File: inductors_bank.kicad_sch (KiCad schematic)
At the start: 38 parts, among them K501 HF3F-L-12-1ZL2T, K502 HF3F-L-12-1ZL2T, K503 HF3F-L-12-1ZL2T, K504 HF3F-L-12-1ZL2T, K505 HF3F-L-12-1ZL2T, K506 HF3F-L-12-1ZL2T, K507 HF3F-L-12-1ZL2T, Q501 PMOS, Q502 PMOS, Q503 NMOS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

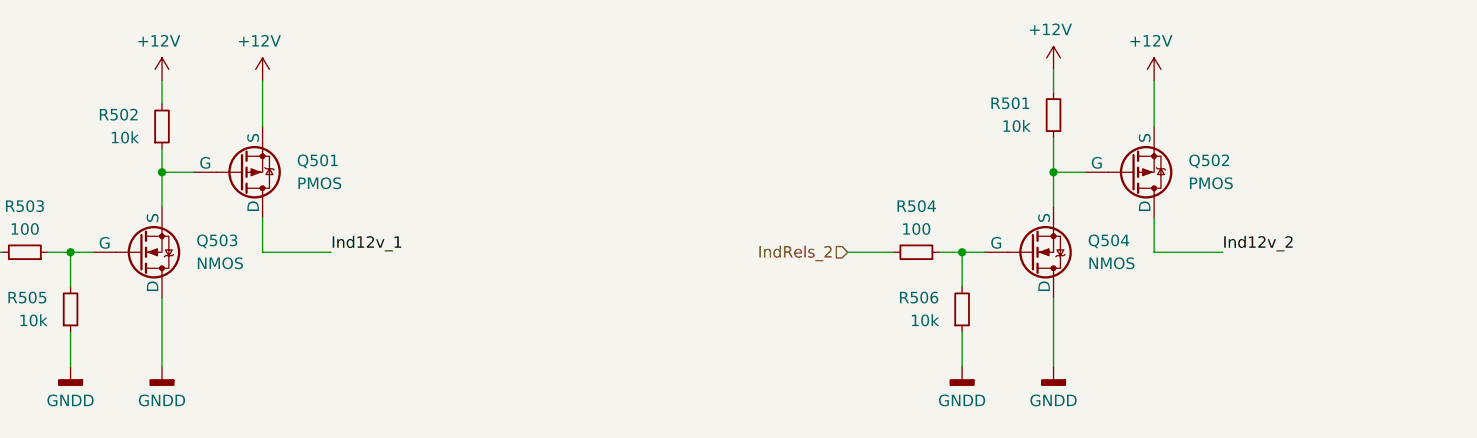
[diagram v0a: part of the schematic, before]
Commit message: Many more vias, improved some routing
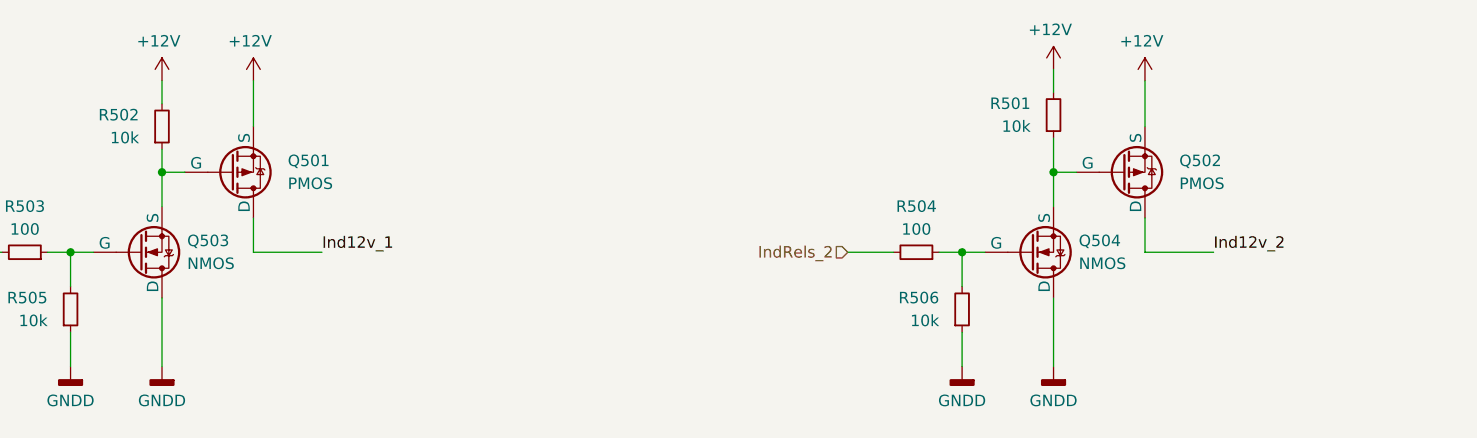
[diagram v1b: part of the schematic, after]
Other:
- moved on the sheet: Q501, Q502
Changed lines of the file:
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@@
 	(wire
 		(pts
-			(xy 211.836 57.15) (xy 211.836 62.23)
+			(xy 210.82 57.15) (xy 210.82 62.23)
 		)
 		(stroke
@@
 	(wire
 		(pts
-			(xy 112.776 57.15) (xy 112.776 62.23)
+			(xy 111.76 57.15) (xy 111.76 62.23)
 		)
 		(stroke
@@
 	(wire
 		(pts
-			(xy 211.836 76.2) (xy 211.836 72.39)
+			(xy 210.82 76.2) (xy 210.82 72.39)
 		)
 		(stroke
@@
 	(wire
 		(pts
-			(xy 204.216 67.31) (xy 200.66 67.31)
+			(xy 203.2 67.31) (xy 200.66 67.31)
 		)
 		(stroke
@@
 	(wire
 		(pts
-			(xy 105.156 67.31) (xy 101.6 67.31)
+			(xy 104.14 67.31) (xy 101.6 67.31)
 		)
 		(stroke
@@
 	(wire
 		(pts
-			(xy 120.396 76.2) (xy 112.776 76.2)
+			(xy 119.38 76.2) (xy 111.76 76.2)
 		)
 		(stroke
@@
 	(wire
 		(pts
-			(xy 219.456 76.2) (xy 211.836 76.2)
+			(xy 218.44 76.2) (xy 210.82 76.2)
 		)
 		(stroke
@@
 	(wire
 		(pts
-			(xy 112.776 76.2) (xy 112.776 72.39)
+			(xy 111.76 76.2) (xy 111.76 72.39)
 		)
 		(stroke
@@
 	)
 	(label "Ind12v_2"
-		(at 219.456 76.2 0)
+		(at 218.44 76.2 0)
 		(fields_autoplaced yes)
 		(effects
@@
 	)
 	(label "Ind12v_1"
-		(at 120.396 76.2 0)
+		(at 119.38 76.2 0)
 		(fields_autoplaced yes)
 		(effects
@@
 		(on_board yes)
 		(dnp no)
-		(fields_autoplaced yes)
 		(property "Reference" "Q504"
-			(at 204.47 74.9299 0)
+			(at 203.454 74.9299 0)
 			(effects
 				(font
@@
 		)
 		(property "Value" "NMOS"
-			(at 204.47 77.4699 0)
+			(at 203.454 77.4699 0)
 			(effects
 				(font
@@
 	(symbol
 		(lib_id "power:+12V")
-		(at 112.776 57.15 0)
+		(at 111.76 57.15 0)
 		(mirror y)
 		(unit 1)
@@
 		(dnp no)
 		(property "Reference" "#PWR0503"
-			(at 112.776 60.96 0)
+			(at 111.76 60.96 0)
 			(effects
 				(font
@@
 		)
 		(property "Value" "+12V"
-			(at 112.395 52.7558 0)
+			(at 111.379 52.7558 0)
 			(effects
 				(font
@@
 		)
 		(property "Footprint" ""
-			(at 112.776 57.15 0)
+			(at 111.76 57.15 0)
 			(effects
 				(font
@@
 		)
 		(property "Datasheet" ""
-			(at 112.776 57.15 0)
+			(at 111.76 57.15 0)
 			(effects
 				(font
@@
 		)
 		(property "Description" "Power symbol creates a global label with name \"+12V\""
-			(at 112.776 57.15 0)
+			(at 111.76 57.15 0)
 			(effects
 				(font
@@
 	(symbol
 		(lib_id "Simulation_SPICE:PMOS")
-		(at 209.296 67.31 0)
+		(at 208.28 67.31 0)
 		(mirror x)
 		(unit 1)
@@
 		(fields_autoplaced yes)
 		(property "Reference" "Q502"
-			(at 215.646 66.0399 0)
+			(at 214.63 66.0399 0)
 			(effects
 				(font
@@
 		)
 		(property "Value" "PMOS"
-			(at 215.646 68.5799 0)
+			(at 214.63 68.5799 0)
 			(effects
 				(font
@@
 		)
 		(property "Footprint" "Package_TO_SOT_SMD:SOT-23"
-			(at 214.376 69.85 0)
+			(at 213.36 69.85 0)
 			(effects
 				(font
@@
 		)
 		(property "Datasheet" "https://ngspice.sourceforge.io/docs/ngspice-html-manual/manual.xhtml#cha_MOSFETs"
-			(at 209.296 54.61 0)
+			(at 208.28 54.61 0)
 			(effects
 				(font
@@
 		)
 		(property "Description" "P-MOSFET transistor, drain/source/gate"
-			(at 209.296 67.31 0)
+			(at 208.28 67.31 0)
 			(effects
 				(font
@@
 		)
 		(property "Sim.Device" "PMOS"
-			(at 209.296 50.165 0)
+			(at 208.28 50.165 0)
 			(effects
 				(font
@@
 		)
 		(property "Sim.Type" "VDMOS"
-			(at 209.296 48.26 0)
+			(at 208.28 48.26 0)
 			(effects
 				(font
@@
 		)
 		(property "Sim.Pins" "1=D 2=G 3=S"
-			(at 209.296 52.07 0)
+			(at 208.28 52.07 0)
 			(effects
 				(font
@@
 	(symbol
 		(lib_id "Simulation_SPICE:PMOS")
-		(at 110.236 67.31 0)
+		(at 109.22 67.31 0)
 		(mirror x)
 		(unit 1)
@@
 		(fields_autoplaced yes)
 		(property "Reference" "Q501"
-			(at 116.586 66.0399 0)
+			(at 115.57 66.0399 0)
 			(effects
 				(font
@@
 		)
 		(property "Value" "PMOS"
-			(at 116.586 68.5799 0)
+			(at 115.57 68.5799 0)
 			(effects
 				(font
@@
 		)
 		(property "Footprint" "Package_TO_SOT_SMD:SOT-23"
-			(at 115.316 69.85 0)
+			(at 114.3 69.85 0)
 			(effects
 				(font
@@
 		)
 		(property "Datasheet" "https://ngspice.sourceforge.io/docs/ngspice-html-manual/manual.xhtml#cha_MOSFETs"
-			(at 110.236 54.61 0)
+			(at 109.22 54.61 0)
 			(effects
 				(font
@@
 		)
 		(property "Description" "P-MOSFET transistor, drain/source/gate"
-			(at 110.236 67.31 0)
+			(at 109.22 67.31 0)
 			(effects
 				(font
@@
 		)
 		(property "Sim.Device" "PMOS"
-			(at 110.236 50.165 0)
+			(at 109.22 50.165 0)
 			(effects
 				(font
@@
 		)
 		(property "Sim.Type" "VDMOS"
-			(at 110.236 48.26 0)
+			(at 109.22 48.26 0)
 			(effects
 				(font
@@
 		)
 		(property "Sim.Pins" "1=D 2=G 3=S"
-			(at 110.236 52.07 0)
+			(at 109.22 52.07 0)
 			(effects
 				(font
@@
 	(symbol
 		(lib_id "power:+12V")
-		(at 211.836 57.15 0)
+		(at 210.82 57.15 0)
 		(mirror y)
 		(unit 1)
@@
 		(dnp no)
 		(property "Reference" "#PWR0504"
-			(at 211.836 60.96 0)
+			(at 210.82 60.96 0)
 			(effects
 				(font
@@
 		)
 		(property "Value" "+12V"
-			(at 211.455 52.7558 0)
+			(at 210.439 52.7558 0)
 			(effects
 				(font
@@
 		)
 		(property "Footprint" ""
-			(at 211.836 57.15 0)
+			(at 210.82 57.15 0)
 			(effects
 				(font
@@
 		)
 		(property "Datasheet" ""
-			(at 211.836 57.15 0)
+			(at 210.82 57.15 0)
 			(effects
 				(font
@@
 		)
 		(property "Description" "Power symbol creates a global label with name \"+12V\""
-			(at 211.836 57.15 0)
+			(at 210.82 57.15 0)
 			(effects
 				(font
@@
 		(on_board yes)
 		(dnp no)
-		(fields_autoplaced yes)
 		(property "Reference" "Q503"
-			(at 105.41 74.9299 0)
+			(at 104.394 74.9299 0)
 			(effects
 				(font
@@
 		)
 		(property "Value" "NMOS"
-			(at 105.41 77.4699 0)
+			(at 104.394 77.4699 0)
 			(effects
 				(font

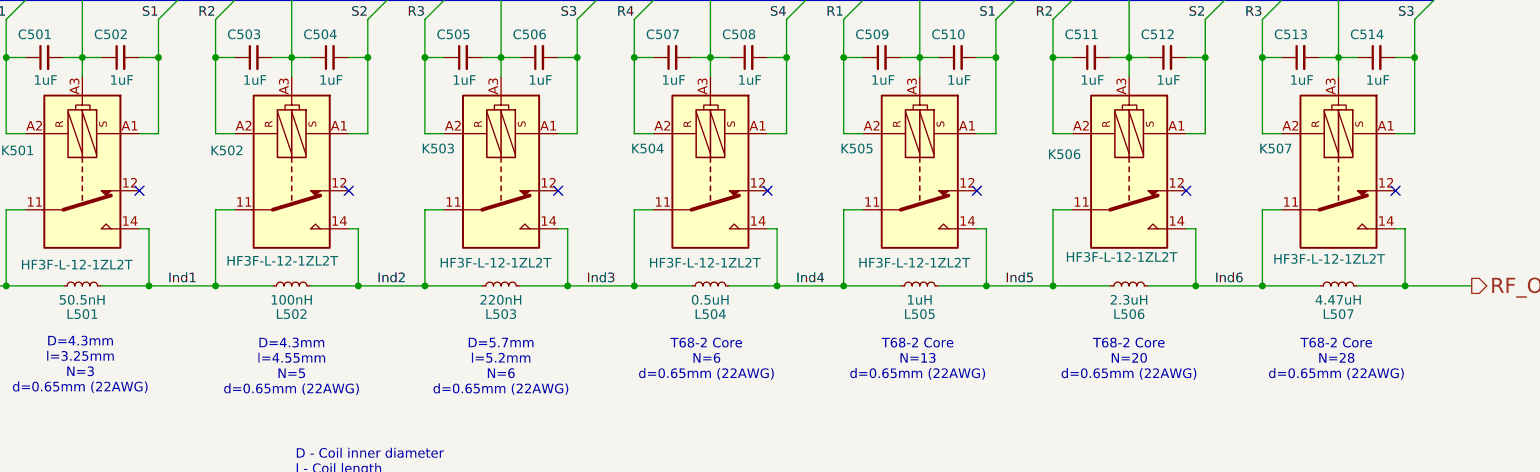
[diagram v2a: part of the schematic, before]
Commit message: Improve RF routing
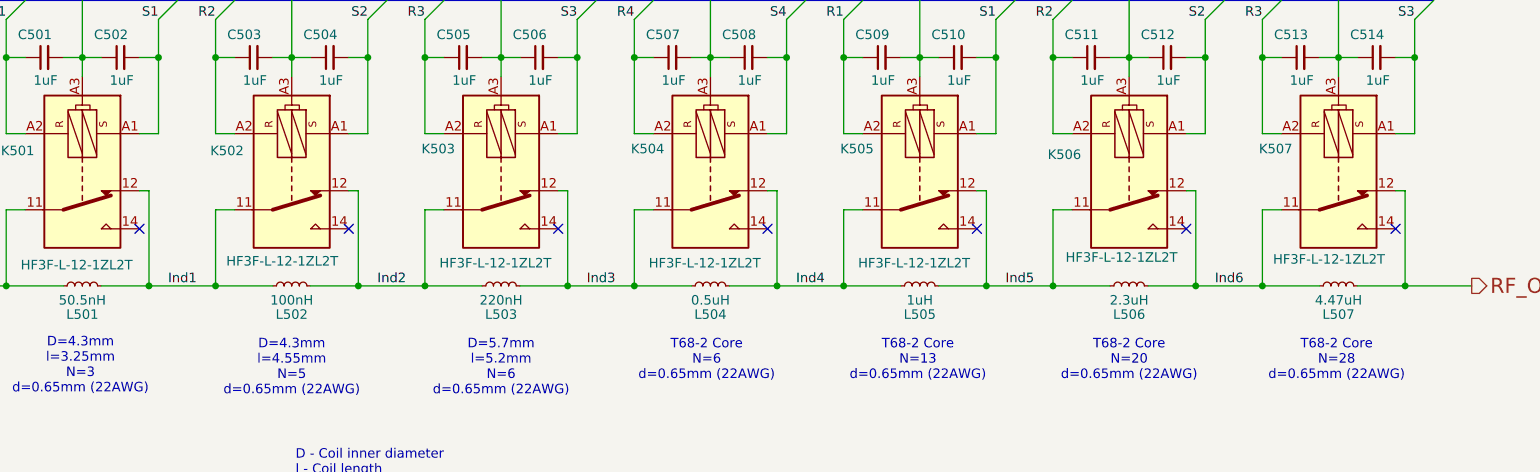
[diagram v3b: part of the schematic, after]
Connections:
- net Ind1: now also K501.12; no longer K501.14
- net Ind2: now also K502.12; no longer K502.14
- net Ind3: now also K503.12; no longer K503.14
- net Ind4: now also K504.12; no longer K504.14
- net Ind5: now also K505.12; no longer K505.14
- net Ind6: now also K506.12; no longer K506.14
- net RF_Out: now also K507.12; no longer K507.14

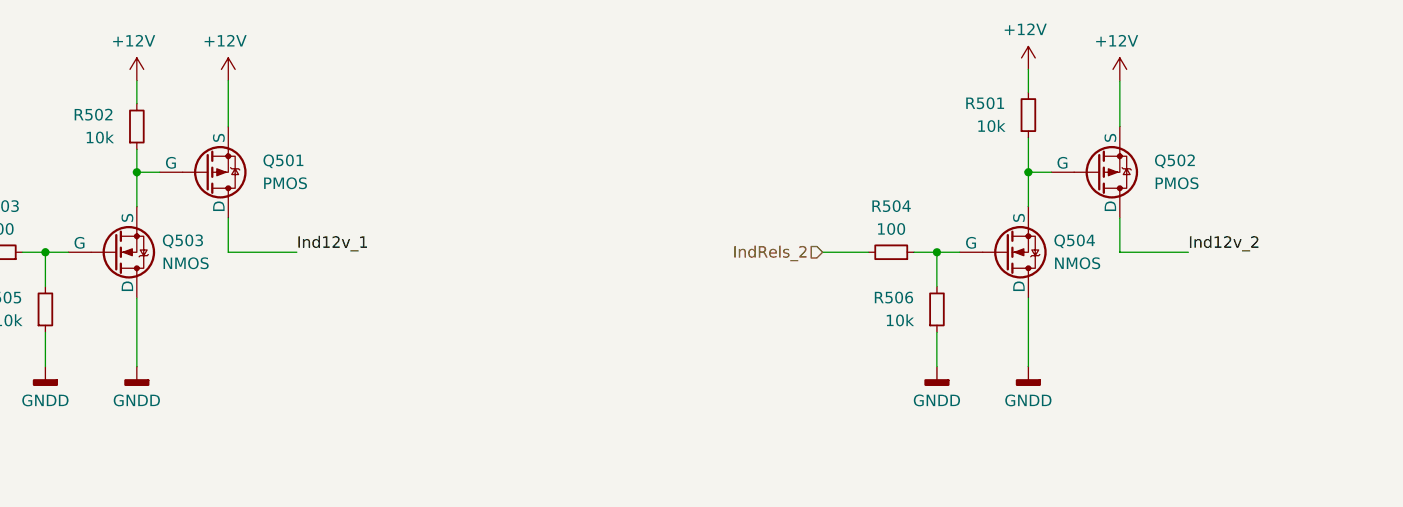
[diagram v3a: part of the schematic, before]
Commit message: Added transistors parts. Added reverse polarity protection, pending adding to layout
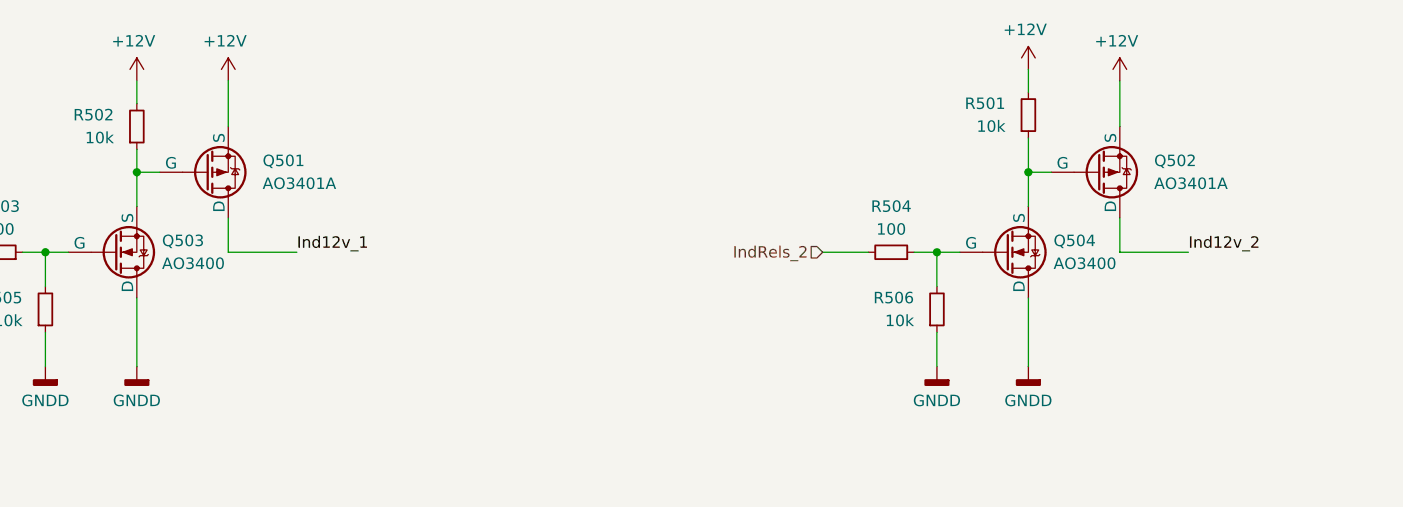
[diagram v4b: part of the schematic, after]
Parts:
- Q501, Q502: value PMOS -> AO3401A
- Q503, Q504: value NMOS -> AO3400
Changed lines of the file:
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@@
 			)
 		)
-		(property "Value" "NMOS"
+		(property "Value" "AO3400"
 			(at 203.454 77.4699 0)
 			(effects
@@
 			)
 		)
-		(property "Datasheet" "https://ngspice.sourceforge.io/docs/ngspice-html-manual/manual.xhtml#cha_MOSFETs"
+		(property "Datasheet" "~"
 			(at 198.12 63.5 0)
 			(effects
@@
 			)
 		)
-		(property "Value" "PMOS"
+		(property "Value" "AO3401A"
 			(at 214.63 68.5799 0)
 			(effects
@@
 			)
 		)
-		(property "Datasheet" "https://ngspice.sourceforge.io/docs/ngspice-html-manual/manual.xhtml#cha_MOSFETs"
+		(property "Datasheet" "~"
 			(at 208.28 54.61 0)
 			(effects
@@
 			)
 		)
-		(property "Value" "PMOS"
+		(property "Value" "AO3401A"
 			(at 115.57 68.5799 0)
 			(effects
@@
 			)
 		)
-		(property "Datasheet" "https://ngspice.sourceforge.io/docs/ngspice-html-manual/manual.xhtml#cha_MOSFETs"
+		(property "Datasheet" "~"
 			(at 109.22 54.61 0)
 			(effects
@@
 			)
 		)
-		(property "Value" "NMOS"
+		(property "Value" "AO3400"
 			(at 104.394 77.4699 0)
 			(effects
@@
 			)
 		)
-		(property "Datasheet" "https://ngspice.sourceforge.io/docs/ngspice-html-manual/manual.xhtml#cha_MOSFETs"
+		(property "Datasheet" "~"
 			(at 99.06 63.5 0)
 			(effects

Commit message: A0 Production. Updated to KiCad 9.0.x
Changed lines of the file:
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@@
 (kicad_sch
-	(version 20231120)
+	(version 20250114)
 	(generator "eeschema")
-	(generator_version "8.0")
+	(generator_version "9.0")
 	(paper "A4")
 	(title_block
@@
 		(company "TiZed")
 	)
+	(text "D=5.7mm\nl=5.2mm\nN=6\nd=0.65mm (22AWG)"
+		(exclude_from_sim no)
+		(at 118.11 158.242 0)
+		(effects
+			(font
+				(size 1.27 1.27)
+			)
+		)
+	)
+	(text "D=4.3mm\nl=4.55mm\nN=5\nd=0.65mm (22AWG)"
+		(exclude_from_sim no)
+		(at 90.17 158.242 0)
+		(effects
+			(font
+				(size 1.27 1.27)
+			)
+		)
+	)
+	(text "D=4.3mm\nl=3.25mm\nN=3\nd=0.65mm (22AWG)"
+		(exclude_from_sim no)
+		(at 61.976 157.988 0)
+		(effects
+			(font
+				(size 1.27 1.27)
+			)
+		)
+	)
+	(text "T68-2 Core\nN=6\nd=0.65mm (22AWG)"
+		(exclude_from_sim no)
+		(at 145.542 157.226 0)
+		(effects
+			(font
+				(size 1.27 1.27)
+			)
+		)
+	)
+	(text "D - Coil inner diameter\nl - Coil length\nN - Number of coil turns\nd - Magnetic wire diameter"
+		(exclude_from_sim no)
+		(at 90.678 172.974 0)
+		(effects
+			(font
+				(size 1.27 1.27)
+			)
+			(justify left)
+		)
+	)
+	(text "T68-2 Core\nN=28\nd=0.65mm (22AWG)"
+		(exclude_from_sim no)
+		(at 229.616 157.226 0)
+		(effects
+			(font
+				(size 1.27 1.27)
+			)
+		)
+	)
+	(text "T68-2 Core\nN=20\nd=0.65mm (22AWG)"
+		(exclude_from_sim no)
+		(at 201.93 157.226 0)
+		(effects
+			(font
+				(size 1.27 1.27)
+			)
+		)
+	)
+	(text "T68-2 Core\nN=13\nd=0.65mm (22AWG)"
+		(exclude_from_sim no)
+		(at 173.736 157.226 0)
+		(effects
+			(font
+				(size 1.27 1.27)
+			)
+		)
+	)
 	(junction
 		(at 156.21 116.84)
@@
 		)
 	)
-	(text "D=5.7mm\nl=5.2mm\nN=6\nd=0.65mm (22AWG)"
-		(exclude_from_sim no)
-		(at 118.11 158.242 0)
-		(effects
-			(font
-				(size 1.27 1.27)
-			)
-		)
-	)
-	(text "D=4.3mm\nl=4.55mm\nN=5\nd=0.65mm (22AWG)"
-		(exclude_from_sim no)
-		(at 90.17 158.242 0)
-		(effects
-			(font
-				(size 1.27 1.27)
-			)
-		)
-	)
-	(text "D=4.3mm\nl=3.25mm\nN=3\nd=0.65mm (22AWG)"
-		(exclude_from_sim no)
-		(at 61.976 157.988 0)
-		(effects
-			(font
-				(size 1.27 1.27)
-			)
-		)
-	)
-	(text "T68-2 Core\nN=6\nd=0.65mm (22AWG)"
-		(exclude_from_sim no)
-		(at 145.542 157.226 0)
-		(effects
-			(font
-				(size 1.27 1.27)
-			)
-		)
-	)
-	(text "D - Coil inner diameter\nl - Coil length\nN - Number of coil turns\nd - Magnetic wire diameter"
-		(exclude_from_sim no)
-		(at 90.678 172.974 0)
-		(effects
-			(font
-				(size 1.27 1.27)
-			)
-			(justify left)
-		)
-	)
-	(text "T68-2 Core\nN=28\nd=0.65mm (22AWG)"
-		(exclude_from_sim no)
-		(at 229.616 157.226 0)
-		(effects
-			(font
-				(size 1.27 1.27)
-			)
-		)
-	)
-	(text "T68-2 Core\nN=20\nd=0.65mm (22AWG)"
-		(exclude_from_sim no)
-		(at 201.93 157.226 0)
-		(effects
-			(font
-				(size 1.27 1.27)
-			)
-		)
-	)
-	(text "T68-2 Core\nN=13\nd=0.65mm (22AWG)"
-		(exclude_from_sim no)
-		(at 173.736 157.226 0)
-		(effects
-			(font
-				(size 1.27 1.27)
-			)
-		)
-	)
 	(label "S2"
 		(at 212.09 111.76 180)
-		(fields_autoplaced yes)
 		(effects
 			(font
@@
 	(label "R1"
 		(at 52.07 111.76 180)
-		(fields_autoplaced yes)
 		(effects
 			(font
@@
 	(label "Ind12v_2"
 		(at 218.44 76.2 0)
-		(fields_autoplaced yes)
 		(effects
 			(font
@@
 	(label "Ind5"
 		(at 185.42 147.32 0)
-		(fields_autoplaced yes)
 		(effects
 			(font
@@
 	(label "Ind1"
 		(at 73.66 147.32 0)
-		(fields_autoplaced yes)
 		(effects
 			(font
@@
 	(label "R1"
 		(at 163.83 111.76 180)
-		(fields_autoplaced yes)
 		(effects
 			(font
@@
 	(label "R2"
 		(at 80.01 111.76 180)
-		(fields_autoplaced yes)
 		(effects
 			(font
@@
 	(label "Ind6"
 		(at 213.36 147.32 0)
-		(fields_autoplaced yes)
 		(effects
 			(font
@@
 	(label "Ind2"
 		(at 101.6 147.32 0)
-		(fields_autoplaced yes)
 		(effects
 			(font
@@
 	(label "Ind4"
 		(at 157.48 147.32 0)
-		(fields_autoplaced yes)
 		(effects
 			(font
@@
 	(label "S4"
 		(at 156.21 111.76 180)
-		(fields_autoplaced yes)
 		(effects
 			(font
@@
 	(label "Ind3"
 		(at 129.54 147.32 0)
-		(fields_autoplaced yes)
 		(effects
 			(font
@@
 	(label "Ind12v_1"
 		(at 119.38 76.2 0)
-		(fields_autoplaced yes)
 		(effects
 			(font
@@
 	(label "R2"
 		(at 191.77 111.76 180)
-		(fields_autoplaced yes)
 		(effects
 			(font
@@
 	(label "S3"
 		(at 128.27 111.76 180)
-		(fields_autoplaced yes)
 		(effects
 			(font
@@
 	(label "S1"
 		(at 184.15 111.76 180)
-		(fields_autoplaced yes)
 		(effects
 			(font
@@
 	(label "R3"
 		(at 219.71 111.76 180)
-		(fields_autoplaced yes)
 		(effects
 			(font
@@
 	(label "Ind12v_1"
 		(at 55.88 106.68 180)
-		(fields_autoplaced yes)
 		(effects
 			(font
@@
 	(label "S3"
 		(at 240.03 111.76 180)
-		(fields_autoplaced yes)
 		(effects
 			(font
@@
 	(label "R4"
 		(at 135.89 111.76 180)
-		(fields_autoplaced yes)
 		(effects
 			(font
@@
 	(label "S2"
 		(at 100.33 111.76 180)
-		(fields_autoplaced yes)
 		(effects
 			(font
@@
 	(label "S1"
 		(at 72.39 111.76 180)
-		(fields_autoplaced yes)
 		(effects
 			(font
@@
 	(label "Ind12v_2"
 		(at 167.64 106.68 180)
-		(fields_autoplaced yes)
 		(effects
 			(font
@@
 	(label "R3"
 		(at 107.95 111.76 180)
-		(fields_autoplaced yes)
 		(effects
 			(font
@@
 		(shape input)
 		(at 43.18 109.22 180)
-		(fields_autoplaced yes)
 		(effects
 			(font
@@
 		(shape input)
 		(at 177.8 76.2 180)
-		(fields_autoplaced yes)
 		(effects
 			(font
@@
 		(shape input)
 		(at 43.18 147.32 180)
-		(fields_autoplaced yes)
 		(effects
 			(font
@@
 		(shape input)
 		(at 78.74 76.2 180)
-		(fields_autoplaced yes)
 		(effects
 			(font
@@
 		(shape output)
 		(at 247.65 147.32 0)
-		(fields_autoplaced yes)
-		(effects
-			(font
+		(effects
+			(font
